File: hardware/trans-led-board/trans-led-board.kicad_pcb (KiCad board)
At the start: 2 copper layers, 15 x 9 mm, 4 parts, among them J1 Conn_01x02

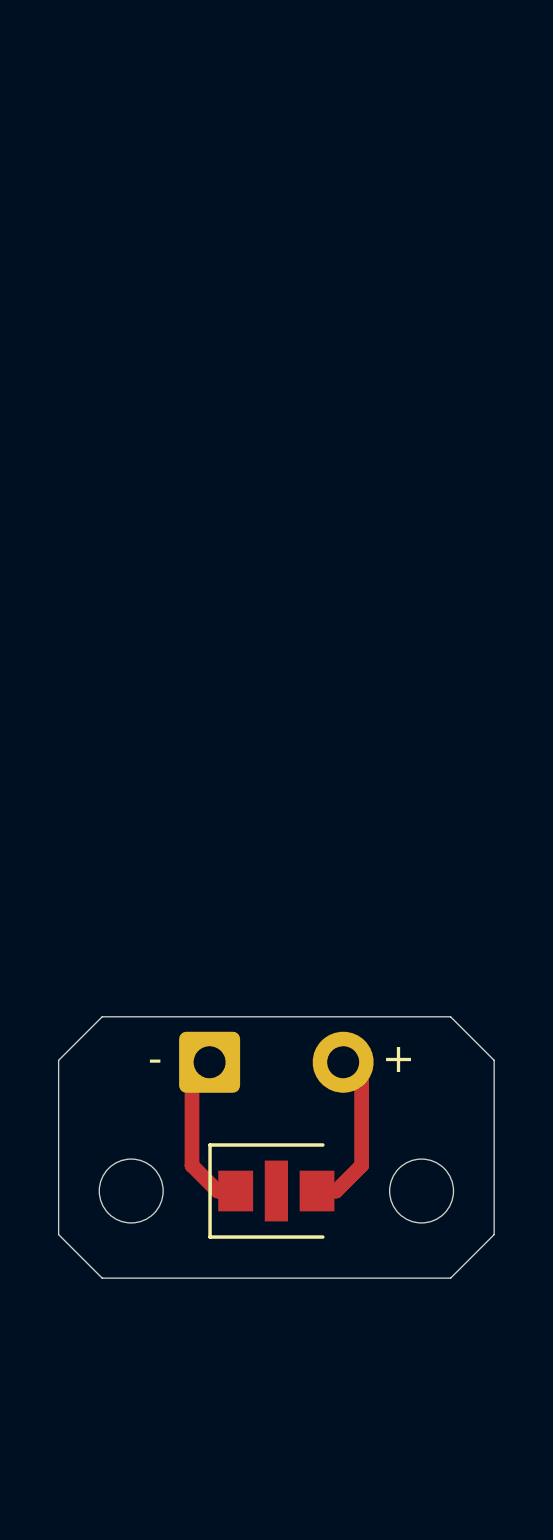
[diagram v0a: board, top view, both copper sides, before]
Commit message: Updated transmission LED board design
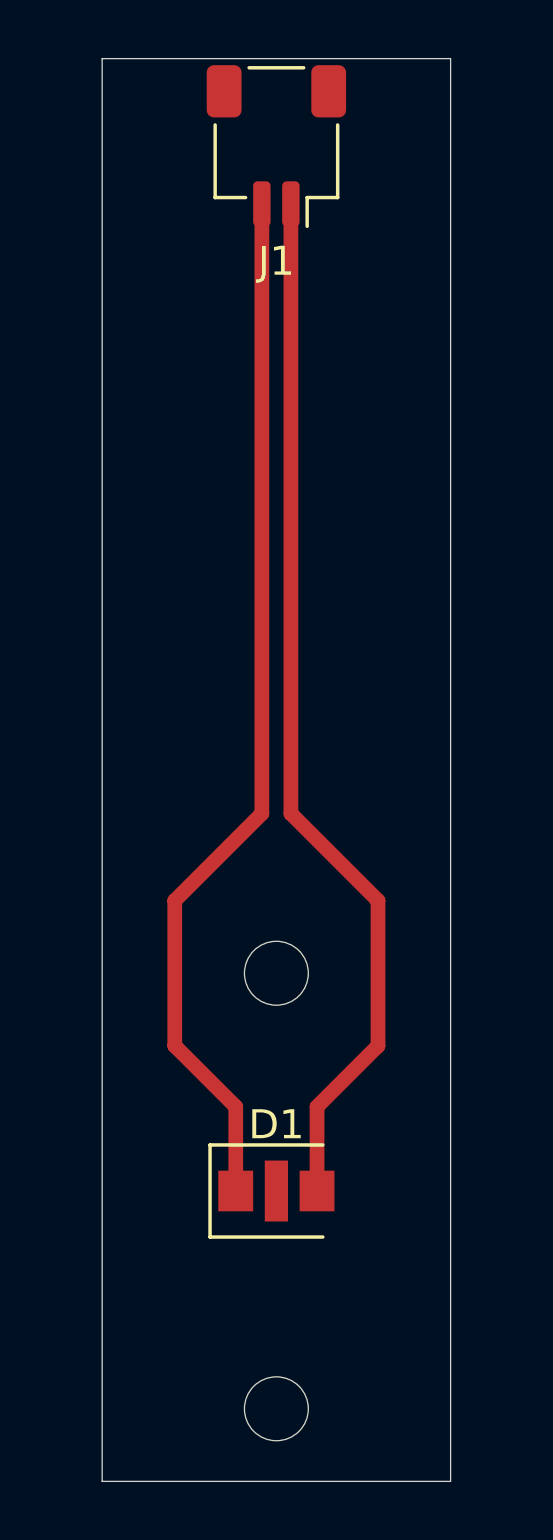
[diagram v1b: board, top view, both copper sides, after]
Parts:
- J1: footprint Connector_Wire:SolderWire-0.5sqmm_1x02_P4.6mm_D0.9mm_OD2.1mm -> Connector_JST:JST_SH_SM02B-SRSS-TB_1x02-1MP_P1.00mm_Horizontal
- moved J1 31.6 mm to (120.0, 44.0), turned to 180 degrees
- moved H1 9.01 mm to (120.0, 87.5)
- moved H2 9.01 mm to (120.0, 72.5)
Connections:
- J1 pad 1: Net-(D1-Pad1) -> Net-(D1-Pad2)
- J1 pad 2: Net-(D1-Pad2) -> Net-(D1-Pad1)
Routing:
- net Net-(D1-Pad1): track 5.68 -> 36.1 mm
- net Net-(D1-Pad2): track 5.72 -> 36.1 mm
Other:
- board size 15 x 9 mm -> 12 x 49 mm
- board text removed: "+"
- board text removed: "-"

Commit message: Fixed size of transmission LED board
Mistakenly used diameter as the radius of the reference circles.
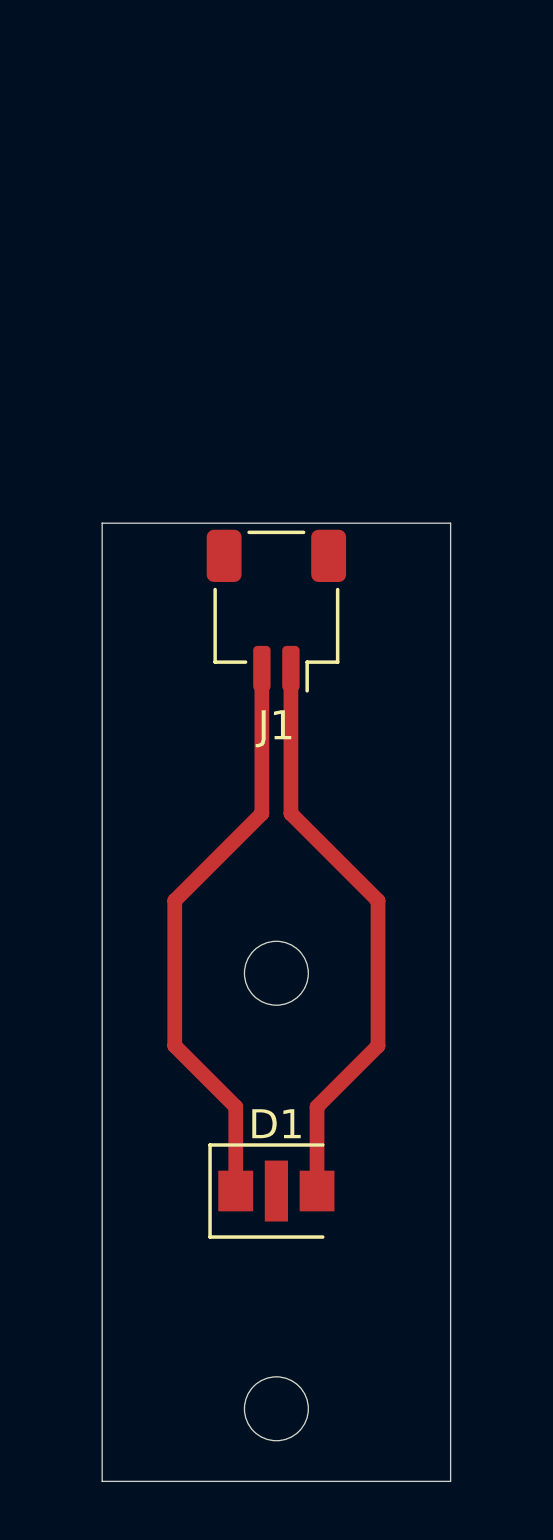
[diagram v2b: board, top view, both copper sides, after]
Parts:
- moved J1 16.0 mm to (120.0, 60.0)
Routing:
- net Net-(D1-Pad2): track 36.1 -> 20.1 mm
- net Net-(D1-Pad1): track 36.1 -> 20.1 mm
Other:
- board size 12 x 49 mm -> 12 x 33 mm
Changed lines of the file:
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@@
   )
   (module Connector_JST:JST_SH_SM02B-SRSS-TB_1x02-1MP_P1.00mm_Horizontal (layer F.Cu)
-    (at 120 44 180)
+    (at 120 60 180)
     (descr "JST SH series connector, SM02B-SRSS-TB (http://www.jst-mfg.com/product/pdf/eng/eSH.pdf), generated with kicad-footprint-generator")
     (tags "connector JST SH top entry")
@@
       (effects (font (size 1 1) (thickness 0.15)))
     )
+    (fp_line (start -0.5 -0.967893) (end 0 -1.675) (layer F.Fab) (width 0.1))
+    (fp_line (start -1 -1.675) (end -0.5 -0.967893) (layer F.Fab) (width 0.1))
+    (fp_line (start 2.9 -3.28) (end -2.9 -3.28) (layer F.CrtYd) (width 0.05))
+    (fp_line (start 2.9 3.28) (end 2.9 -3.28) (layer F.CrtYd) (width 0.05))
+    (fp_line (start -2.9 3.28) (end 2.9 3.28) (layer F.CrtYd) (width 0.05))
+    (fp_line (start -2.9 -3.28) (end -2.9 3.28) (layer F.CrtYd) (width 0.05))
+    (fp_line (start 2 -1.675) (end 2 2.575) (layer F.Fab) (width 0.1))
+    (fp_line (start -2 -1.675) (end -2 2.575) (layer F.Fab) (width 0.1))
+    (fp_line (start -2 2.575) (end 2 2.575) (layer F.Fab) (width 0.1))
+    (fp_line (start -0.94 2.685) (end 0.94 2.685) (layer F.SilkS) (width 0.12))
+    (fp_line (start 2.11 -1.785) (end 1.06 -1.785) (layer F.SilkS) (width 0.12))
+    (fp_line (start 2.11 0.715) (end 2.11 -1.785) (layer F.SilkS) (width 0.12))
+    (fp_line (start -1.06 -1.785) (end -1.06 -2.775) (layer F.SilkS) (width 0.12))
+    (fp_line (start -2.11 -1.785) (end -1.06 -1.785) (layer F.SilkS) (width 0.12))
+    (fp_line (start -2.11 0.715) (end -2.11 -1.785) (layer F.SilkS) (width 0.12))
+    (fp_line (start -2 -1.675) (end 2 -1.675) (layer F.Fab) (width 0.1))
     (fp_text user %R (at 0 0) (layer F.Fab)
       (effects (font (size 1 1) (thickness 0.15)))
     )
-    (fp_line (start -2 -1.675) (end 2 -1.675) (layer F.Fab) (width 0.1))
-    (fp_line (start -2.11 0.715) (end -2.11 -1.785) (layer F.SilkS) (width 0.12))
-    (fp_line (start -2.11 -1.785) (end -1.06 -1.785) (layer F.SilkS) (width 0.12))
-    (fp_line (start -1.06 -1.785) (end -1.06 -2.775) (layer F.SilkS) (width 0.12))
-    (fp_line (start 2.11 0.715) (end 2.11 -1.785) (layer F.SilkS) (width 0.12))
-    (fp_line (start 2.11 -1.785) (end 1.06 -1.785) (layer F.SilkS) (width 0.12))
-    (fp_line (start -0.94 2.685) (end 0.94 2.685) (layer F.SilkS) (width 0.12))
-    (fp_line (start -2 2.575) (end 2 2.575) (layer F.Fab) (width 0.1))
-    (fp_line (start -2 -1.675) (end -2 2.575) (layer F.Fab) (width 0.1))
-    (fp_line (start 2 -1.675) (end 2 2.575) (layer F.Fab) (width 0.1))
-    (fp_line (start -2.9 -3.28) (end -2.9 3.28) (layer F.CrtYd) (width 0.05))
-    (fp_line (start -2.9 3.28) (end 2.9 3.28) (layer F.CrtYd) (width 0.05))
-    (fp_line (start 2.9 3.28) (end 2.9 -3.28) (layer F.CrtYd) (width 0.05))
-    (fp_line (start 2.9 -3.28) (end -2.9 -3.28) (layer F.CrtYd) (width 0.05))
-    (fp_line (start -1 -1.675) (end -0.5 -0.967893) (layer F.Fab) (width 0.1))
-    (fp_line (start -0.5 -0.967893) (end 0 -1.675) (layer F.Fab) (width 0.1))
     (pad MP smd roundrect (at 1.8 1.875 180) (size 1.2 1.8) (layers F.Cu F.Paste F.Mask) (roundrect_rratio 0.208333))
     (pad MP smd roundrect (at -1.8 1.875 180) (size 1.2 1.8) (layers F.Cu F.Paste F.Mask) (roundrect_rratio 0.208333))
@@
       (effects (font (size 1 1) (thickness 0.15)))
     )
+    (fp_line (start -1.6 -0.625) (end -1.6 1.25) (layer F.Fab) (width 0.1))
+    (fp_line (start -1.6 1.25) (end 1.6 1.25) (layer F.Fab) (width 0.1))
+    (fp_line (start 1.6 -1.25) (end -0.975 -1.25) (layer F.Fab) (width 0.1))
+    (fp_line (start -0.975 -1.25) (end -1.6 -0.625) (layer F.Fab) (width 0.1))
+    (fp_line (start 1.6 1.25) (end 1.6 -1.25) (layer F.Fab) (width 0.1))
+    (fp_line (start -2.28 1.58) (end -2.28 -1.58) (layer F.CrtYd) (width 0.05))
+    (fp_line (start -2.28 -1.58) (end 2.28 -1.58) (layer F.CrtYd) (width 0.05))
+    (fp_line (start 2.28 -1.58) (end 2.28 1.58) (layer F.CrtYd) (width 0.05))
+    (fp_line (start 2.28 1.58) (end -2.28 1.58) (layer F.CrtYd) (width 0.05))
+    (fp_line (start -2.285 -1.585) (end -2.285 1.585) (layer F.SilkS) (width 0.12))
+    (fp_line (start -2.285 1.585) (end 1.6 1.585) (layer F.SilkS) (width 0.12))
     (fp_line (start 1.6 -1.585) (end -2.285 -1.585) (layer F.SilkS) (width 0.12))
-    (fp_line (start -2.285 1.585) (end 1.6 1.585) (layer F.SilkS) (width 0.12))
-    (fp_line (start -2.285 -1.585) (end -2.285 1.585) (layer F.SilkS) (width 0.12))
-    (fp_line (start 2.28 1.58) (end -2.28 1.58) (layer F.CrtYd) (width 0.05))
-    (fp_line (start 2.28 -1.58) (end 2.28 1.58) (layer F.CrtYd) (width 0.05))
-    (fp_line (start -2.28 -1.58) (end 2.28 -1.58) (layer F.CrtYd) (width 0.05))
-    (fp_line (start -2.28 1.58) (end -2.28 -1.58) (layer F.CrtYd) (width 0.05))
-    (fp_line (start 1.6 1.25) (end 1.6 -1.25) (layer F.Fab) (width 0.1))
-    (fp_line (start -0.975 -1.25) (end -1.6 -0.625) (layer F.Fab) (width 0.1))
-    (fp_line (start 1.6 -1.25) (end -0.975 -1.25) (layer F.Fab) (width 0.1))
-    (fp_line (start -1.6 1.25) (end 1.6 1.25) (layer F.Fab) (width 0.1))
-    (fp_line (start -1.6 -0.625) (end -1.6 1.25) (layer F.Fab) (width 0.1))
     (fp_text user %R (at 0 0) (layer F.Fab)
       (effects (font (size 0.8 0.8) (thickness 0.12)))
@@
       (effects (font (size 1 1) (thickness 0.15)))
     )
+    (fp_circle (center 0 0) (end 2.45 0) (layer F.CrtYd) (width 0.05))
     (fp_circle (center 0 0) (end 2.2 0) (layer Cmts.User) (width 0.15))
-    (fp_circle (center 0 0) (end 2.45 0) (layer F.CrtYd) (width 0.05))
     (fp_text user %R (at 0.3 0) (layer F.Fab)
       (effects (font (size 1 1) (thickness 0.15)))
@@
       (effects (font (size 1 1) (thickness 0.15)))
     )
+    (fp_circle (center 0 0) (end 2.45 0) (layer F.CrtYd) (width 0.05))
     (fp_circle (center 0 0) (end 2.2 0) (layer Cmts.User) (width 0.15))
-    (fp_circle (center 0 0) (end 2.45 0) (layer F.CrtYd) (width 0.05))
     (fp_text user %R (at 0.3 0) (layer F.Fab)
       (effects (font (size 1 1) (thickness 0.15)))
@@
     (pad 1 np_thru_hole circle (at 0 0) (size 2.2 2.2) (drill 2.2) (layers *.Cu *.Mask))
   )
-  (dimension 49 (width 0.15) (layer Cmts.User)
-    (gr_text "49.000 mm" (at 111.2 65.5 90) (layer Cmts.User)
+  (dimension 33 (width 0.15) (layer Cmts.User)
+    (gr_text "33.000 mm" (at 111.2 73.5 90) (layer Cmts.User)
       (effects (font (size 1 1) (thickness 0.15)))
     )
-    (feature1 (pts (xy 114 41) (xy 111.913579 41)))
+    (feature1 (pts (xy 114 57) (xy 111.913579 57)))
     (feature2 (pts (xy 114 90) (xy 111.913579 90)))
-    (crossbar (pts (xy 112.5 90) (xy 112.5 41)))
-    (arrow1a (pts (xy 112.5 41) (xy 113.086421 42.126504)))
-    (arrow1b (pts (xy 112.5 41) (xy 111.913579 42.126504)))
+    (crossbar (pts (xy 112.5 90) (xy 112.5 57)))
+    (arrow1a (pts (xy 112.5 57) (xy 113.086421 58.126504)))
+    (arrow1b (pts (xy 112.5 57) (xy 111.913579 58.126504)))
     (arrow2a (pts (xy 112.5 90) (xy 113.086421 88.873496)))
     (arrow2b (pts (xy 112.5 90) (xy 111.913579 88.873496)))
@@
     (arrow2b (pts (xy 114 91.499999) (xy 115.126504 90.913578)))
   )
-  (gr_line (start 114 41) (end 114 90) (layer Edge.Cuts) (width 0.0381))
-  (gr_line (start 126 41) (end 114 41) (layer Edge.Cuts) (width 0.0381))
-  (gr_line (start 126 90) (end 126 41) (layer Edge.Cuts) (width 0.0381))
+  (gr_line (start 114 57) (end 114 90) (layer Edge.Cuts) (width 0.0381))
+  (gr_line (start 126 57) (end 114 57) (layer Edge.Cuts) (width 0.0381))
+  (gr_line (start 126 90) (end 126 57) (layer Edge.Cuts) (width 0.0381))
   (gr_line (start 114 90) (end 126 90) (layer Edge.Cuts) (width 0.0381))
-  (gr_circle (center 120 80) (end 162.5 80) (layer Cmts.User) (width 0.15))
-  (gr_circle (center 120 80) (end 152 80) (layer Cmts.User) (width 0.15))
-  (gr_circle (center 120 80) (end 125 80) (layer Cmts.User) (width 0.15))
+  (gr_circle (center 120 80) (end 141.3 80) (layer Cmts.User) (width 0.15))
+  (gr_circle (center 120 80) (end 136 80) (layer Cmts.User) (width 0.15))
+  (gr_circle (center 120 80) (end 122.5 80) (layer Cmts.User) (width 0.15))
   (gr_line (start 118 80) (end 122 80) (layer B.SilkS) (width 0.1524))
   (gr_line (start 120 78) (end 120 82) (layer B.SilkS) (width 0.1524))
   (gr_circle (center 120 80) (end 122 80) (layer B.SilkS) (width 0.1524))
-  (segment (start 120.5 67) (end 120.5 46) (width 0.508) (layer F.Cu) (net 1))
   (segment (start 123.5 70) (end 120.5 67) (width 0.508) (layer F.Cu) (net 1))
   (segment (start 123.5 75) (end 123.5 70) (width 0.508) (layer F.Cu) (net 1))
   (segment (start 121.4 77.1) (end 123.5 75) (width 0.508) (layer F.Cu) (net 1))
   (segment (start 121.4 80) (end 121.4 77.1) (width 0.508) (layer F.Cu) (net 1))
-  (segment (start 119.5 67) (end 119.5 46) (width 0.508) (layer F.Cu) (net 2))
+  (segment (start 120.5 67) (end 120.5 62) (width 0.508) (layer F.Cu) (net 1))
   (segment (start 116.5 75) (end 116.5 70) (width 0.508) (layer F.Cu) (net 2))
   (segment (start 116.5 70) (end 119.5 67) (width 0.508) (layer F.Cu) (net 2))
   (segment (start 118.6 77.1) (end 116.5 75) (width 0.508) (layer F.Cu) (net 2))
   (segment (start 118.6 80) (end 118.6 77.1) (width 0.508) (layer F.Cu) (net 2))
+  (segment (start 119.5 67) (end 119.5 62) (width 0.508) (layer F.Cu) (net 2))
 )

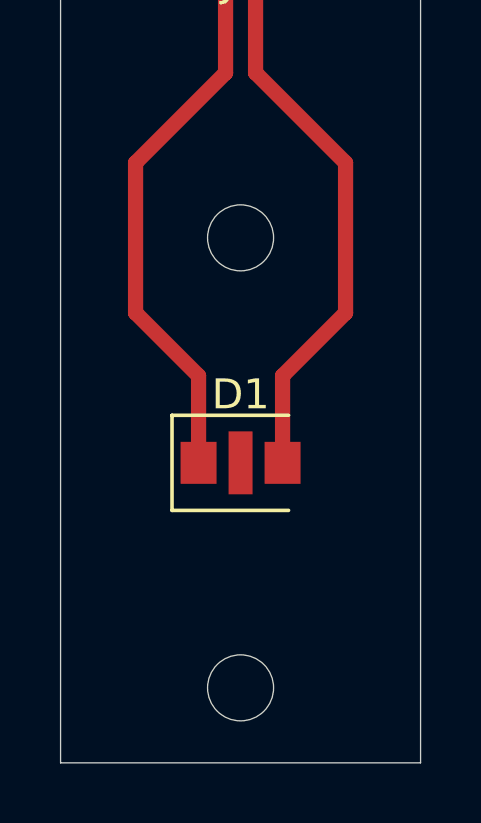
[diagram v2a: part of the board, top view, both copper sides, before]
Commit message: Various silkscreen updates
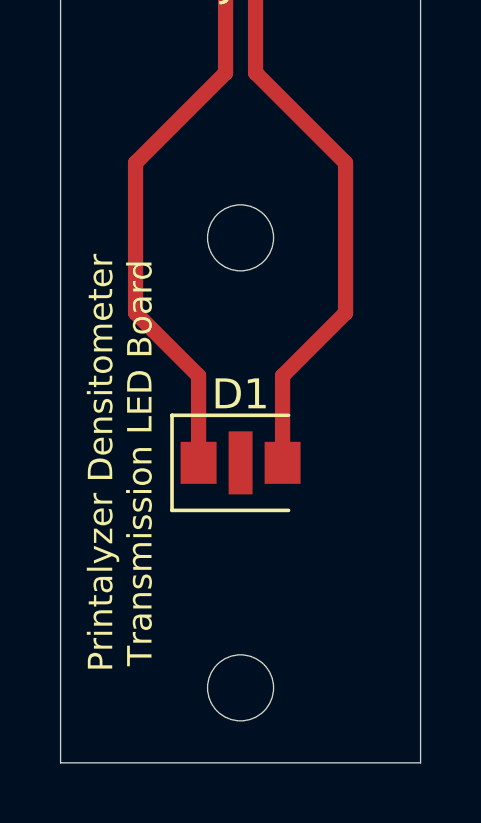
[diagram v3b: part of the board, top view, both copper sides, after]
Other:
- board text added: "Main Board"
- board text added: "Printalyzer Densitometer Transmission LED Board"
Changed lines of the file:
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@@
   (general
     (thickness 1.6)
-    (drawings 12)
+    (drawings 18)
     (tracks 10)
     (zones 0)
@@
   )
   (setup
-    (last_trace_width 0.508)
+    (last_trace_width 0.254)
     (user_trace_width 0.127)
     (user_trace_width 0.254)
@@
     (pad 1 np_thru_hole circle (at 0 0) (size 2.2 2.2) (drill 2.2) (layers *.Cu *.Mask))
   )
+  (dimension 17.5 (width 0.15) (layer Cmts.User)
+    (gr_text "17.500 mm" (at 134.3 81.25 90) (layer Cmts.User)
+      (effects (font (size 1 1) (thickness 0.15)))
+    )
+    (feature1 (pts (xy 126 72.5) (xy 133.586421 72.5)))
+    (feature2 (pts (xy 126 90) (xy 133.586421 90)))
+    (crossbar (pts (xy 133 90) (xy 133 72.5)))
+    (arrow1a (pts (xy 133 72.5) (xy 133.586421 73.626504)))
+    (arrow1b (pts (xy 133 72.5) (xy 132.413579 73.626504)))
+    (arrow2a (pts (xy 133 90) (xy 133.586421 88.873496)))
+    (arrow2b (pts (xy 133 90) (xy 132.413579 88.873496)))
+  )
+  (dimension 10 (width 0.15) (layer Cmts.User)
+    (gr_text "10.000 mm" (at 131.8 85 90) (layer Cmts.User)
+      (effects (font (size 1 1) (thickness 0.15)))
+    )
+    (feature1 (pts (xy 126 80) (xy 131.086421 80)))
+    (feature2 (pts (xy 126 90) (xy 131.086421 90)))
+    (crossbar (pts (xy 130.5 90) (xy 130.5 80)))
+    (arrow1a (pts (xy 130.5 80) (xy 131.086421 81.126504)))
+    (arrow1b (pts (xy 130.5 80) (xy 129.913579 81.126504)))
+    (arrow2a (pts (xy 130.5 90) (xy 131.086421 88.873496)))
+    (arrow2b (pts (xy 130.5 90) (xy 129.913579 88.873496)))
+  )
+  (dimension 2.5 (width 0.15) (layer Cmts.User)
+    (gr_text "2.500 mm" (at 128.8 88.75 90) (layer Cmts.User)
+      (effects (font (size 1 1) (thickness 0.15)))
+    )
+    (feature1 (pts (xy 126 87.5) (xy 128.086421 87.5)))
+    (feature2 (pts (xy 126 90) (xy 128.086421 90)))
+    (crossbar (pts (xy 127.5 90) (xy 127.5 87.5)))
+    (arrow1a (pts (xy 127.5 87.5) (xy 128.086421 88.626504)))
+    (arrow1b (pts (xy 127.5 87.5) (xy 126.913579 88.626504)))
+    (arrow2a (pts (xy 127.5 90) (xy 128.086421 88.873496)))
+    (arrow2b (pts (xy 127.5 90) (xy 126.913579 88.873496)))
+  )
+  (gr_text "Printalyzer Densitometer\nTransmission LED Board" (at 116 80 90) (layer B.SilkS)
+    (effects (font (size 0.8128 0.8128) (thickness 0.1524)) (justify mirror))
+  )
+  (gr_text "Main Board" (at 120.015 60.071 180) (layer B.SilkS)
+    (effects (font (size 0.8128 0.8128) (thickness 0.1524)) (justify mirror))
+  )
+  (gr_text "Printalyzer Densitometer\nTransmission LED Board" (at 116 80 90) (layer F.SilkS)
+    (effects (font (size 0.8128 0.8128) (thickness 0.1524)))
+  )
   (dimension 33 (width 0.15) (layer Cmts.User)
